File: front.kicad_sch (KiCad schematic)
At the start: 26 parts, among them J1 776087-1, SW1 SW_Push, SW2 SW_SPST, SW3 SW_Push, SW4 SW_Push

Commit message: Minor changes, change to v9.0
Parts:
- removed APP1, APP2: Conn_01x03, symbol Connector_Generic:Conn_01x03
- added APPS: Conn_01x04, symbol Connector_Generic:Conn_01x04
- DSH3: value No Connector -> Superseal 1.5
- renumbered DSH5 to DSH1, DSH1 to DSH5, J1 to TCU
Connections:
- net APPS-PWR: now also APPS.1 (Pin_1)
- net APPS-SIG1: now also APPS.2 (Pin_2)
- net APPS-SIG2: now also APPS.3 (Pin_3)
- net STEP-1+: no longer TCU.12 (Pin_12)
- new net APPS-GND: APPS.4 (Pin_4), TCU.12 (Pin_12)
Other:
- note added: "BOTH APPSs WILL BE WIRED INTO THIS SINGLE CONNECTOR"
- note added: "FIREWALL CONNECTOR HDP26-24-31PE Pinout: 1 MiscPWR 2 StepperPWR 3 LVMSPWR 4 IdleCtrl 5 Blip 6 TPS Power 1 7 TPS Signal 1 8 TPS Ground 1 9 TPS Power 2 10 TPS Signal 2 11 TPS Ground 2 12 Stepper 1+ 13 Stepper 1- 14 Stepper 2+ 15 Stepper 2- 16 Neutral 17 Shift Down 18 Shift Up 19 Tachometer 20 Shutdown Out 21 Starter Sig 22 Fan Sig 23 BLS Sig 24 Launch Sig 25 Launch LED 26 27 28 29 CANH 30 CANL 31 S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"
- note added: "Power Signal 1 Signal 2 Ground"
- note removed: "Power Signal Ground"

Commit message: Remove LVMSPwr, replace with MiscPwr
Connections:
- net LVMSPWR is gone; now on net MiscPWR: BTS1.1 (Pin_1)
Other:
- note added: "FIREWALL CONNECTOR HDP26-24-31PE Pinout: 1 MiscPWR 2 StepperPWR 3 4 IdleCtrl 5 Blip 6 TPS Power 1 7 TPS Signal 1 8 TPS Ground 1 9 TPS Power 2 10 TPS Signal 2 11 TPS Ground 2 12 Stepper 1+ 13 Stepper 1- 14 Stepper 2+ 15 Stepper 2- 16 Neutral 17 Shift Down 18 Shift Up 19 Tachometer 20 Shutdown Out 21 Starter Sig 22 Fan Sig 23 BLS Sig 24 Launch Sig 25 Launch LED 26 27 28 29 CANH 30 CANL 31 SENGND"
- note removed: "FIREWALL CONNECTOR HDP26-24-31PE Pinout: 1 MiscPWR 2 StepperPWR 3 LVMSPWR 4 IdleCtrl 5 Blip 6 TPS Power 1 7 TPS Signal 1 8 TPS Ground 1 9 TPS Power 2 10 TPS Signal 2 11 TPS Ground 2 12 Stepper 1+ 13 Stepper 1- 14 Stepper 2+ 15 Stepper 2- 16 Neutral 17 Shift Down 18 Shift Up 19 Tachometer 20 Shutdown Out 21 Starter Sig 22 Fan Sig 23 BLS Sig 24 Launch Sig 25 Launch LED 26 27 28 29 CANH 30 CANL 31 S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"

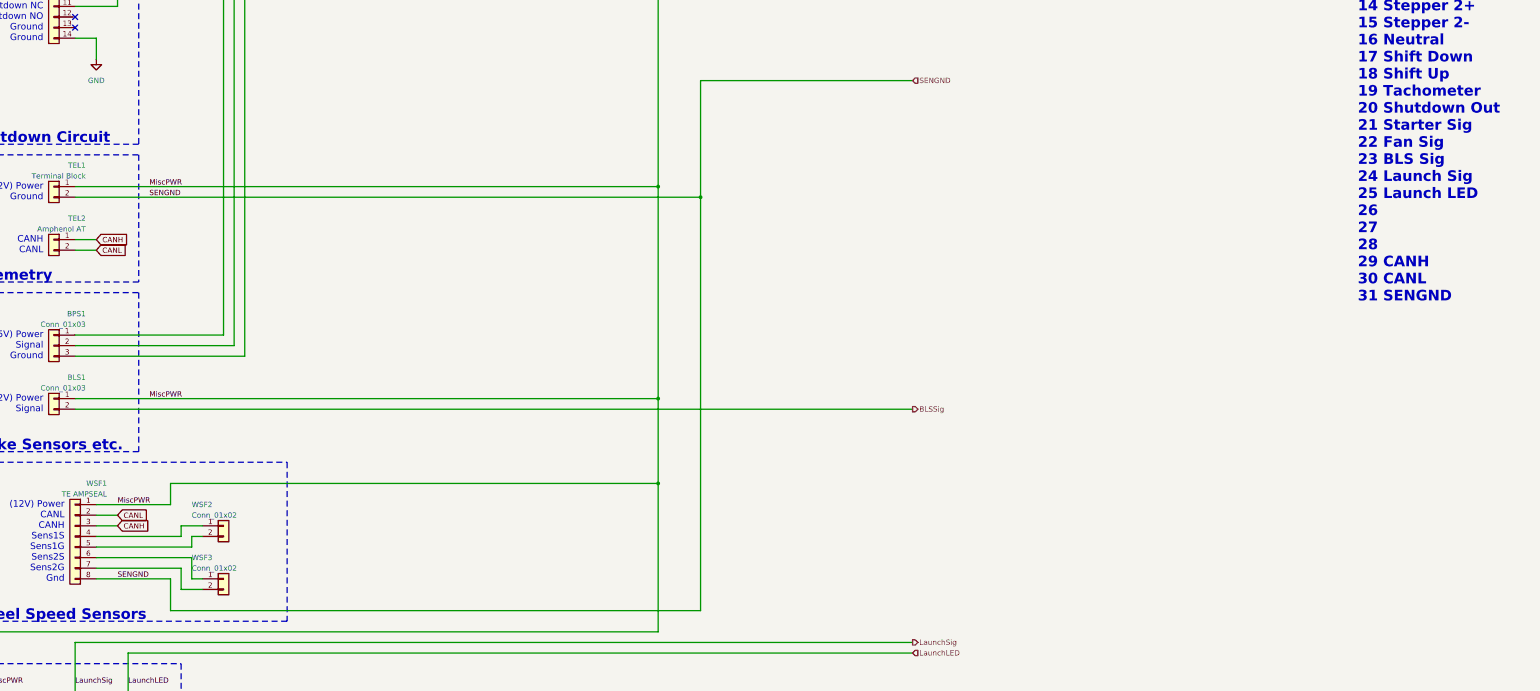
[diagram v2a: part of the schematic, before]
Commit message: Remove SENGND from front of loom
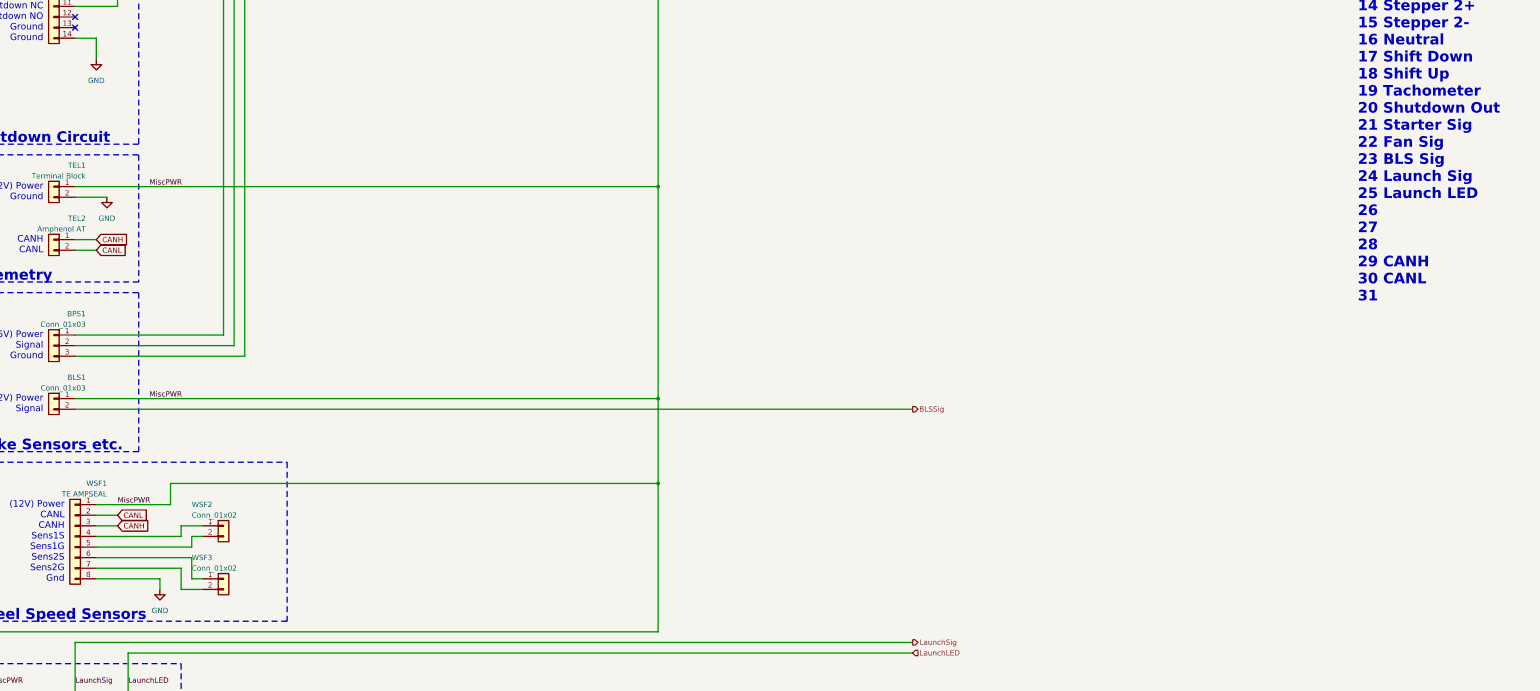
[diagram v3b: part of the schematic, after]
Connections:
- net SENGND is gone; now on net GND: TEL1.2 (Pin_2), WSF1.8 (Pin_8)
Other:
- note added: "FIREWALL CONNECTOR HDP26-24-31PE Pinout: 1 MiscPWR 2 StepperPWR 3 4 IdleCtrl 5 Blip 6 TPS Power 1 7 TPS Signal 1 8 TPS Ground 1 9 TPS Power 2 10 TPS Signal 2 11 TPS Ground 2 12 Stepper 1+ 13 Stepper 1- 14 Stepper 2+ 15 Stepper 2- 16 Neutral 17 Shift Down 18 Shift Up 19 Tachometer 20 Shutdown Out 21 Starter Sig 22 Fan Sig 23 BLS Sig 24 Launch Sig 25 Launch LED 26 27 28 29 CANH 30 CANL 31"
- note removed: "FIREWALL CONNECTOR HDP26-24-31PE Pinout: 1 MiscPWR 2 StepperPWR 3 4 IdleCtrl 5 Blip 6 TPS Power 1 7 TPS Signal 1 8 TPS Ground 1 9 TPS Power 2 10 TPS Signal 2 11 TPS Ground 2 12 Stepper 1+ 13 Stepper 1- 14 Stepper 2+ 15 Stepper 2- 16 Neutral 17 Shift Down 18 Shift Up 19 Tachometer 20 Shutdown Out 21 Starter Sig 22 Fan Sig 23 BLS Sig 24 Launch Sig 25 Launch LED 26 27 28 29 CANH 30 CANL 31 SENGND"
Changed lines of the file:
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@@
 		)
 	)
-	(text "FIREWALL CONNECTOR\nHDP26-24-31PE\n\nPinout:\n 1 MiscPWR\n 2 StepperPWR\n 3 \n 4 IdleCtrl\n 5 Blip\n 6 TPS Power 1\n 7 TPS Signal 1\n 8 TPS Ground 1\n 9 TPS Power 2\n10 TPS Signal 2\n11 TPS Ground 2\n12 Stepper 1+\n13 Stepper 1-\n14 Stepper 2+\n15 Stepper 2-\n16 Neutral\n17 Shift Down\n18 Shift Up\n19 Tachometer\n20 Shutdown Out\n21 Starter Sig\n22 Fan Sig\n23 BLS Sig\n24 Launch Sig\n25 Launch LED\n26 \n27 \n28 \n29 CANH\n30 CANL\n31 SENGND"
+	(text "FIREWALL CONNECTOR\nHDP26-24-31PE\n\nPinout:\n 1 MiscPWR\n 2 StepperPWR\n 3 \n 4 IdleCtrl\n 5 Blip\n 6 TPS Power 1\n 7 TPS Signal 1\n 8 TPS Ground 1\n 9 TPS Power 2\n10 TPS Signal 2\n11 TPS Ground 2\n12 Stepper 1+\n13 Stepper 1-\n14 Stepper 2+\n15 Stepper 2-\n16 Neutral\n17 Shift Down\n18 Shift Up\n19 Tachometer\n20 Shutdown Out\n21 Starter Sig\n22 Fan Sig\n23 BLS Sig\n24 Launch Sig\n25 Launch LED\n26 \n27 \n28 \n29 CANH\n30 CANL\n31"
 		(exclude_from_sim no)
 		(at 347.98 208.28 0)
@@
 		(color 0 0 0 0)
 	)
-	(junction
-		(at 190.5 254)
-		(diameter 0)
-		(color 0 0 0 0)
-	)
 	(no_connect
 		(at 40.64 213.36)
@@
 	(wire
 		(pts
+			(xy 40.64 254) (xy 48.26 254)
+		)
+		(stroke
+			(width 0)
+			(type default)
+		)
+	)
+	(wire
+		(pts
 			(xy 63.5 81.28) (xy 241.3 81.28)
 		)
@@
 	(wire
 		(pts
+			(xy 60.96 345.44) (xy 45.72 345.44)
+		)
+		(stroke
+			(width 0)
+			(type default)
+		)
+	)
+	(wire
+		(pts
 			(xy 66.04 342.9) (xy 45.72 342.9)
 		)
@@
 	(wire
 		(pts
-			(xy 190.5 226.06) (xy 241.3 226.06)
-		)
-		(stroke
-			(width 0)
-			(type default)
-			(color 0 0 64 1)
-		)
-	)
-	(wire
-		(pts
 			(xy 35.56 132.08) (xy 48.26 132.08)
 		)
@@
 	(wire
 		(pts
-			(xy 63.5 353.06) (xy 190.5 353.06)
-		)
-		(stroke
-			(width 0)
-			(type default)
-			(color 0 0 64 1)
-		)
-	)
-	(wire
-		(pts
 			(xy 48.26 27.94) (xy 241.3 27.94)
 		)
@@
 	(wire
 		(pts
-			(xy 40.64 254) (xy 190.5 254)
-		)
-		(stroke
-			(width 0)
-			(type default)
-			(color 0 0 64 1)
-		)
-	)
-	(wire
-		(pts
 			(xy 53.34 363.22) (xy 241.3 363.22)
 		)
@@
 	(wire
 		(pts
-			(xy 63.5 345.44) (xy 45.72 345.44)
-		)
-		(stroke
-			(width 0)
-			(type default)
-			(color 0 0 64 1)
-		)
-	)
-	(wire
-		(pts
 			(xy 48.26 55.88) (xy 71.12 55.88)
 		)
@@
 	(wire
 		(pts
-			(xy 63.5 345.44) (xy 63.5 353.06)
-		)
-		(stroke
-			(width 0)
-			(type default)
-			(color 0 0 64 1)
-		)
-	)
-	(wire
-		(pts
-			(xy 190.5 254) (xy 190.5 353.06)
-		)
-		(stroke
-			(width 0)
-			(type default)
-			(color 0 0 64 1)
-		)
-	)
-	(wire
-		(pts
 			(xy 81.28 55.88) (xy 81.28 53.34)
 		)
@@
 	(wire
 		(pts
-			(xy 190.5 254) (xy 190.5 226.06)
-		)
-		(stroke
-			(width 0)
-			(type default)
-			(color 0 0 64 1)
-		)
-	)
-	(wire
-		(pts
 			(xy 40.64 304.8) (xy 241.3 304.8)
 		)
@@
 	(wire
 		(pts
+			(xy 60.96 347.98) (xy 60.96 345.44)
+		)
+		(stroke
+			(width 0)
+			(type default)
+		)
+	)
+	(wire
+		(pts
 			(xy 48.26 20.32) (xy 180.34 20.32)
 		)
@@
 		)
 	)
-	(label "SENGND"
-		(at 58.42 254 0)
-		(effects
-			(font
-				(size 1.27 1.27)
-			)
-			(justify left bottom)
-		)
-	)
 	(label "MiscPWR"
 		(at 58.42 162.56 0)
@@
 		)
 	)
-	(label "SENGND"
-		(at 50.8 345.44 0)
-		(effects
-			(font
-				(size 1.27 1.27)
-			)
-			(justify left bottom)
-		)
-	)
 	(label "ShiftUp"
 		(at 109.22 109.22 0)
@@
 		)
 	)
-	(hierarchical_label "SENGND"
-		(shape input)
-		(at 241.3 226.06 0)
-		(effects
-			(font
-				(size 1.27 1.27)
-			)
-			(justify left)
-		)
-	)
 	(hierarchical_label "STEP-2+"
 		(shape output)
@@
 	)
 	(symbol
+		(lib_id "power:GND")
+		(at 60.96 347.98 0)
+		(unit 1)
+		(exclude_from_sim no)
+		(in_bom yes)
+		(on_board yes)
+		(dnp no)
+		(fields_autoplaced yes)
+		(property "Reference" "#PWR017"
+			(at 60.96 354.33 0)
+			(effects
+				(font
+					(size 1.27 1.27)
+				)
+				(hide yes)
+			)
+		)
+		(property "Value" "GND"
+			(at 60.96 353.06 0)
+			(effects
+				(font
+					(size 1.27 1.27)
+				)
+			)
+		)
+		(property "Footprint" ""
+			(at 60.96 347.98 0)
+			(effects
+				(font
+					(size 1.27 1.27)
+				)
+				(hide yes)
+			)
+		)
+		(property "Datasheet" ""
+			(at 60.96 347.98 0)
+			(effects
+				(font
+					(size 1.27 1.27)
+				)
+				(hide yes)
+			)
+		)
+		(property "Description" "Power symbol creates a global label with name \"GND\" , ground"
+			(at 60.96 347.98 0)
+			(effects
+				(font
+					(size 1.27 1.27)
+				)
+				(hide yes)
+			)
+		)
+		(pin "1"
+		)
+		(instances
+			(project "Loom"
+				(path "/b6ef7529-600a-4e2f-9b83-5120e6f066ed/aac5b161-1a64-4e93-9e42-a89abeb513c7"
+					(reference "#PWR017")
+					(unit 1)
+				)
+			)
+		)
+	)
+	(symbol
 		(lib_id "Connector_Generic:Conn_01x02")
 		(at 35.56 172.72 0)
@@
 					(unit 1)
 				)
+			)
+		)
+	)
+	(symbol
+		(lib_id "power:GND")
+		(at 48.26 254 0)
+		(unit 1)
+		(exclude_from_sim no)
+		(in_bom yes)
+		(on_board yes)
+		(dnp no)
+		(fields_autoplaced yes)
+		(property "Reference" "#PWR016"
+			(at 48.26 260.35 0)
+			(effects
+				(font
+					(size 1.27 1.27)
+				)
+				(hide yes)
+			)
+		)
+		(property "Value" "GND"
+			(at 48.26 259.08 0)
+			(effects
+				(font
+					(size 1.27 1.27)
+				)
+			)
+		)
+		(property "Footprint" ""
+			(at 48.26 254 0)
+			(effects
+				(font
+					(size 1.27 1.27)
+				)
+				(hide yes)
+			)
+		)
+		(property "Datasheet" ""
+			(at 48.26 254 0)
+			(effects
+				(font
+					(size 1.27 1.27)
+				)
+				(hide yes)
+			)
+		)
+		(property "Description" "Power symbol creates a global label with name \"GND\" , ground"
+			(at 48.26 254 0)
+			(effects
+				(font
+					(size 1.27 1.27)
+				)
+				(hide yes)
+			)
+		)
+		(pin "1"
+		)
+		(instances
+			(project "Loom"
+				(path "/b6ef7529-600a-4e2f-9b83-5120e6f066ed/aac5b161-1a64-4e93-9e42-a89abeb513c7"
+					(reference "#PWR016")
+					(unit 1)
+				)

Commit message: Minor changes
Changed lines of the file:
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@@
+	)
+	(rectangle
+		(start 238.76 15.24)
+		(end 261.62 391.16)
+		(stroke
+			(width 0)
+			(type dash)
+		)
+		(fill
+			(type none)
+		)
 	)
 	(rectangle
@@
 	(text "FIREWALL CONNECTOR\nHDP26-24-31PE\n\nPinout:\n 1 MiscPWR\n 2 StepperPWR\n 3 \n 4 IdleCtrl\n 5 Blip\n 6 TPS Power 1\n 7 TPS Signal 1\n 8 TPS Ground 1\n 9 TPS Power 2\n10 TPS Signal 2\n11 TPS Ground 2\n12 Stepper 1+\n13 Stepper 1-\n14 Stepper 2+\n15 Stepper 2-\n16 Neutral\n17 Shift Down\n18 Shift Up\n19 Tachometer\n20 Shutdown Out\n21 Starter Sig\n22 Fan Sig\n23 BLS Sig\n24 Launch Sig\n25 Launch LED\n26 \n27 \n28 \n29 CANH\n30 CANL\n31"
 		(exclude_from_sim no)
-		(at 347.98 208.28 0)
+		(at 261.62 200.66 0)
 		(effects
 			(font

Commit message: Start updating fuses
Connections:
- net MiscPWR: no longer BTS1.1 (Pin_1)
- net at BTS1.2 (Pin_2): now also BSPD1.10 (Pin_10); no longer INS1.1 (Pin_1)
- net at INS1.2 (Pin_2): now also BTS1.1 (Pin_1); no longer BSPD1.10 (Pin_10)
- new net ShutdownPWR: INS1.1 (Pin_1)
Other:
- note added: "FIREWALL CONNECTOR HDP26-24-31PE Pinout: 1 MiscPWR 2 StepperPWR 3 4 IdleCtrl 5 Blip 6 TPS Power 1 7 TPS Signal 1 8 TPS Ground 1 9 TPS Power 2 10 TPS Signal 2 11 TPS Ground 2 12 Stepper 1+ 13 Stepper 1- 14 Stepper 2+ 15 Stepper 2- 16 Neutral 17 Shift Down 18 Shift Up 19 Tachometer 20 Shutdown Out 21 Starter Sig 22 Fan Sig 23 BLS Sig 24 Launch Sig 25 Launch LED 26 27 28 29 CANH 30 CANL 31 Shutdown 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"
- note removed: "FIREWALL CONNECTOR HDP26-24-31PE Pinout: 1 MiscPWR 2 StepperPWR 3 4 IdleCtrl 5 Blip 6 TPS Power 1 7 TPS Signal 1 8 TPS Ground 1 9 TPS Power 2 10 TPS Signal 2 11 TPS Ground 2 12 Stepper 1+ 13 Stepper 1- 14 Stepper 2+ 15 Stepper 2- 16 Neutral 17 Shift Down 18 Shift Up 19 Tachometer 20 Shutdown Out 21 Starter Sig 22 Fan Sig 23 BLS Sig 24 Launch Sig 25 Launch LED 26 27 28 29 CANH 30 CANL 31"
- moved on the sheet: BTS1, INS1
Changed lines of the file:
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@@
 		)
 	)
-	(text "FIREWALL CONNECTOR\nHDP26-24-31PE\n\nPinout:\n 1 MiscPWR\n 2 StepperPWR\n 3 \n 4 IdleCtrl\n 5 Blip\n 6 TPS Power 1\n 7 TPS Signal 1\n 8 TPS Ground 1\n 9 TPS Power 2\n10 TPS Signal 2\n11 TPS Ground 2\n12 Stepper 1+\n13 Stepper 1-\n14 Stepper 2+\n15 Stepper 2-\n16 Neutral\n17 Shift Down\n18 Shift Up\n19 Tachometer\n20 Shutdown Out\n21 Starter Sig\n22 Fan Sig\n23 BLS Sig\n24 Launch Sig\n25 Launch LED\n26 \n27 \n28 \n29 CANH\n30 CANL\n31"
+	(text "FIREWALL CONNECTOR\nHDP26-24-31PE\n\nPinout:\n 1 MiscPWR\n 2 StepperPWR\n 3 \n 4 IdleCtrl\n 5 Blip\n 6 TPS Power 1\n 7 TPS Signal 1\n 8 TPS Ground 1\n 9 TPS Power 2\n10 TPS Signal 2\n11 TPS Ground 2\n12 Stepper 1+\n13 Stepper 1-\n14 Stepper 2+\n15 Stepper 2-\n16 Neutral\n17 Shift Down\n18 Shift Up\n19 Tachometer\n20 Shutdown Out\n21 Starter Sig\n22 Fan Sig\n23 BLS Sig\n24 Launch Sig\n25 Launch LED\n26 \n27 \n28 \n29 CANH\n30 CANL\n31 Shutdown PWR"
 		(exclude_from_sim no)
 		(at 261.62 200.66 0)
@@
 	)
 	(junction
-		(at 180.34 162.56)
-		(diameter 0)
-		(color 0 0 0 0)
-	)
-	(junction
 		(at 180.34 101.6)
 		(diameter 0)
@@
 	(wire
 		(pts
+			(xy 40.64 162.56) (xy 58.42 162.56)
+		)
+		(stroke
+			(width 0)
+			(type default)
+		)
+	)
+	(wire
+		(pts
 			(xy 68.58 335.28) (xy 68.58 337.82)
 		)
@@
 	(wire
 		(pts
-			(xy 180.34 101.6) (xy 180.34 162.56)
+			(xy 180.34 101.6) (xy 180.34 182.88)
 		)
 		(stroke
@@
 	(wire
 		(pts
-			(xy 40.64 162.56) (xy 180.34 162.56)
-		)
-		(stroke
-			(width 0)
-			(type default)
-			(color 255 0 0 1)
-		)
-	)
-	(wire
-		(pts
 			(xy 50.8 332.74) (xy 45.72 332.74)
 		)
@@
 	(wire
 		(pts
-			(xy 180.34 162.56) (xy 180.34 182.88)
-		)
-		(stroke
-			(width 0)
-			(type default)
-			(color 255 0 0 1)
-		)
-	)
-	(wire
-		(pts
 			(xy 104.14 116.84) (xy 114.3 116.84)
 		)
@@
 		)
 	)
-	(label "MiscPWR"
+	(label "ShutdownPWR"
 		(at 58.42 162.56 0)
 		(effects
@@
 		)
 	)
+	(global_label "CANH"
+		(shape input)
+		(at 241.3 378.46 180)
+		(fields_autoplaced yes)
+		(effects
+			(font
+				(size 1.27 1.27)
+				(thickness 0.1588)
+			)
+			(justify right)
+		)
+		(property "Intersheetrefs" "${INTERSHEET_REFS}"
+			(at 233.2952 378.46 0)
+			(effects
+				(font
+					(size 1.27 1.27)
+				)
+				(justify right)
+				(hide yes)
+			)
+		)
+	)
 	(global_label "CANL"
 		(shape input)
@@
 		)
 	)
+	(global_label "CANL"
+		(shape input)
+		(at 241.3 381 180)
+		(fields_autoplaced yes)
+		(effects
+			(font
+				(size 1.27 1.27)
+				(thickness 0.1588)
+			)
+			(justify right)
+		)
+		(property "Intersheetrefs" "${INTERSHEET_REFS}"
+			(at 233.5976 381 0)
+			(effects
+				(font
+					(size 1.27 1.27)
+				)
+				(justify right)
+				(hide yes)
+			)
+		)
+	)
 	(global_label "CANH"
 		(shape input)
@@
 	(hierarchical_label "CANH"
 		(shape bidirectional)
-		(at 241.3 383.54 0)
+		(at 241.3 378.46 0)
 		(effects
 			(font
@@
 	(symbol
 		(lib_id "Connector_Generic:Conn_01x02")
-		(at 35.56 172.72 0)
+		(at 35.56 162.56 0)
 		(mirror y)
 		(unit 1)
@@
 		(dnp no)
 		(property "Reference" "INS1"
-			(at 43.18 167.64 0)
+			(at 43.18 157.48 0)
 			(effects
 				(font
@@
 		)
 		(property "Value" "Conn_01x02"
-			(at 43.18 170.18 0)
+			(at 43.18 160.02 0)
 			(effects
 				(font
@@
 		)
 		(property "Footprint" ""
-			(at 35.56 172.72 0)
+			(at 35.56 162.56 0)
 			(effects
 				(font
@@
 		)
 		(property "Datasheet" "~"
-			(at 35.56 172.72 0)
+			(at 35.56 162.56 0)
 			(effects
 				(font
@@
 		)
 		(property "Description" "Generic connector, single row, 01x02, script generated (kicad-library-utils/schlib/autogen/connector/)"
-			(at 35.56 172.72 0)
+			(at 35.56 162.56 0)
 			(effects
 				(font
@@
 	(symbol
 		(lib_id "Connector_Generic:Conn_01x02")
-		(at 35.56 162.56 0)
+		(at 35.56 172.72 0)
 		(mirror y)
 		(unit 1)
@@
 		(dnp no)
 		(property "Reference" "BTS1"
-			(at 43.18 157.48 0)
+			(at 43.18 167.64 0)
 			(effects
 				(font
@@
 		)
 		(property "Value" "Conn_01x02"
-			(at 43.18 160.02 0)
+			(at 43.18 170.18 0)
 			(effects
 				(font
@@
 		)
 		(property "Footprint" ""
-			(at 35.56 162.56 0)
+			(at 35.56 172.72 0)
 			(effects
 				(font
@@
 		)
 		(property "Datasheet" "~"
-			(at 35.56 162.56 0)
+			(at 35.56 172.72 0)
 			(effects
 				(font
@@
 		)
 		(property "Description" "Generic connector, single row, 01x02, script generated (kicad-library-utils/schlib/autogen/connector/)"
-			(at 35.56 162.56 0)
+			(at 35.56 172.72 0)
 			(effects
 				(font
